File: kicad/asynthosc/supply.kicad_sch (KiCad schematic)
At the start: 37 parts, among them J1 USB_B_Micro, J2 Conn_02x05_Odd_Even, U1 LM1117S-3.3, U11 LM1117S-5.0, U12 Si1869DH, U7 USBLC6-2SC6, U9 LMR62421XMF

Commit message: wip
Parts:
- removed C46: 10u, symbol Device:C
- added C46: 10u, Capacitor_SMD:CP_Elec_4x5.4, symbol Device:C_Polarized
- F1: footprint (none) -> Resistor_SMD:R_0805_2012Metric
- FB1: footprint (none) -> Inductor_SMD:L_0402_1005Metric
- TH1: footprint (none) -> Resistor_THT:R_Axial_DIN0204_L3.6mm_D1.6mm_P7.62mm_Horizontal
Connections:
- net GND: now also C46.2
- net USB_VBUS: now also C46.1
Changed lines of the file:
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@@
 	)
 	(symbol
+		(lib_id "Device:C_Polarized")
+		(at 41.91 180.34 0)
+		(unit 1)
+		(exclude_from_sim no)
+		(in_bom yes)
+		(on_board yes)
+		(dnp no)
+		(fields_autoplaced yes)
+		(property "Reference" "C46"
+			(at 45.72 178.1809 0)
+			(effects
+				(font
+					(size 1.27 1.27)
+				)
+				(justify left)
+			)
+		)
+		(property "Value" "10u"
+			(at 45.72 180.7209 0)
+			(effects
+				(font
+					(size 1.27 1.27)
+				)
+				(justify left)
+			)
+		)
+		(property "Footprint" "Capacitor_SMD:CP_Elec_4x5.4"
+			(at 42.8752 184.15 0)
+			(effects
+				(font
+					(size 1.27 1.27)
+				)
+				(hide yes)
+			)
+		)
+		(property "Datasheet" "~"
+			(at 41.91 180.34 0)
+			(effects
+				(font
+					(size 1.27 1.27)
+				)
+				(hide yes)
+			)
+		)
+		(property "Description" "Polarized capacitor"
+			(at 41.91 180.34 0)
+			(effects
+				(font
+					(size 1.27 1.27)
+				)
+				(hide yes)
+			)
+		)
+		(pin "1"
+		)
+		(pin "2"
+		)
+		(instances
+			(project "asynthosc"
+				(path "/d73e377a-a016-415f-8824-91cc6e4907b9/22ca5166-338c-4a24-8f8a-545e4a0286bf"
+					(reference "C46")
+					(unit 1)
+				)
+			)
+		)
+	)
+	(symbol
 		(lib_id "Device:C")
 		(at 91.44 213.36 0)
@@
 	)
 	(symbol
-		(lib_id "Device:C")
-		(at 41.91 180.34 0)
-		(unit 1)
-		(exclude_from_sim yes)
-		(in_bom yes)
-		(on_board yes)
-		(dnp no)
-		(property "Reference" "C46"
-			(at 34.036 178.816 0)
-			(effects
-				(font
-					(size 1.27 1.27)
-				)
-				(justify left)
-			)
-		)
-		(property "Value" "10u"
-			(at 34.036 181.356 0)
-			(effects
-				(font
-					(size 1.27 1.27)
-				)
-				(justify left)
-			)
-		)
-		(property "Footprint" ""
-			(at 42.8752 184.15 0)
-			(effects
-				(font
-					(size 1.27 1.27)
-				)
-				(hide yes)
-			)
-		)
-		(property "Datasheet" "~"
-			(at 41.91 180.34 0)
-			(effects
-				(font
-					(size 1.27 1.27)
-				)
-				(hide yes)
-			)
-		)
-		(property "Description" "Unpolarized capacitor"
-			(at 41.91 180.34 0)
-			(effects
-				(font
-					(size 1.27 1.27)
-				)
-				(hide yes)
-			)
-		)
-		(pin "2"
-		)
-		(pin "1"
-		)
-		(instances
-			(project "asynthosc"
-				(path "/d73e377a-a016-415f-8824-91cc6e4907b9/22ca5166-338c-4a24-8f8a-545e4a0286bf"
-					(reference "C46")
-					(unit 1)
-				)
-			)
-		)
-	)
-	(symbol
 		(lib_id "Diode:ESD9B5.0ST5G")
 		(at 67.31 57.15 90)
@@
 			)
 		)
-		(property "Footprint" ""
+		(property "Footprint" "Resistor_SMD:R_0805_2012Metric"
 			(at 134.62 44.958 90)
 			(effects
@@
 			)
 		)
-		(property "Footprint" ""
+		(property "Footprint" "Resistor_THT:R_Axial_DIN0204_L3.6mm_D1.6mm_P7.62mm_Horizontal"
 			(at 143.51 43.18 0)
 			(effects
@@
 			)
 		)
-		(property "Footprint" ""
+		(property "Footprint" "Inductor_SMD:L_0402_1005Metric"
 			(at 165.1 44.958 90)
 			(effects

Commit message: sch: change stm32 for smaller one, create smaller jumper footprint
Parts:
- C1, C14, C2, C3, C4, C47, C48, C52, C53, TH1: RefNum (none) -> _generic_
- D1, D3: Manufacturer (none) -> OnSemi
- D17, D18, D7: Manufacturer (none) -> Vishay; RefNum (none) -> SS24
- D2: Manufacturer (none) -> Guangdong
- F1: RefNum ASMD0805-125 -> (none)
- FB1: Manufacturer (none) -> Murata; RefNum (none) -> BLM15PX330SN1D
- J1: Manufacturer (none) -> ShouHan; RefNum (none) -> MicroXNJ
- JP11, JP9: footprint Jumper:SolderJumper-2_P1.3mm_Open_Pad1.0x1.5mm -> Resistor_SMD:R_0402_1005Metric
- L1: Manufacturer (none) -> Xiangru
- U1: Manufacturer (none) -> TI; RefNum (none) -> LM1117S-3.3
- U11: Manufacturer (none) -> Diodes Inc; RefNum (none) -> ZLDO1117
- U12: RefNum (none) -> Si1869DH
- U7: Manufacturer (none) -> ST; RefNum (none) -> USBLC6-2SC6
- U9: Manufacturer (none) -> TI; RefNum (none) -> LMR62421XMF

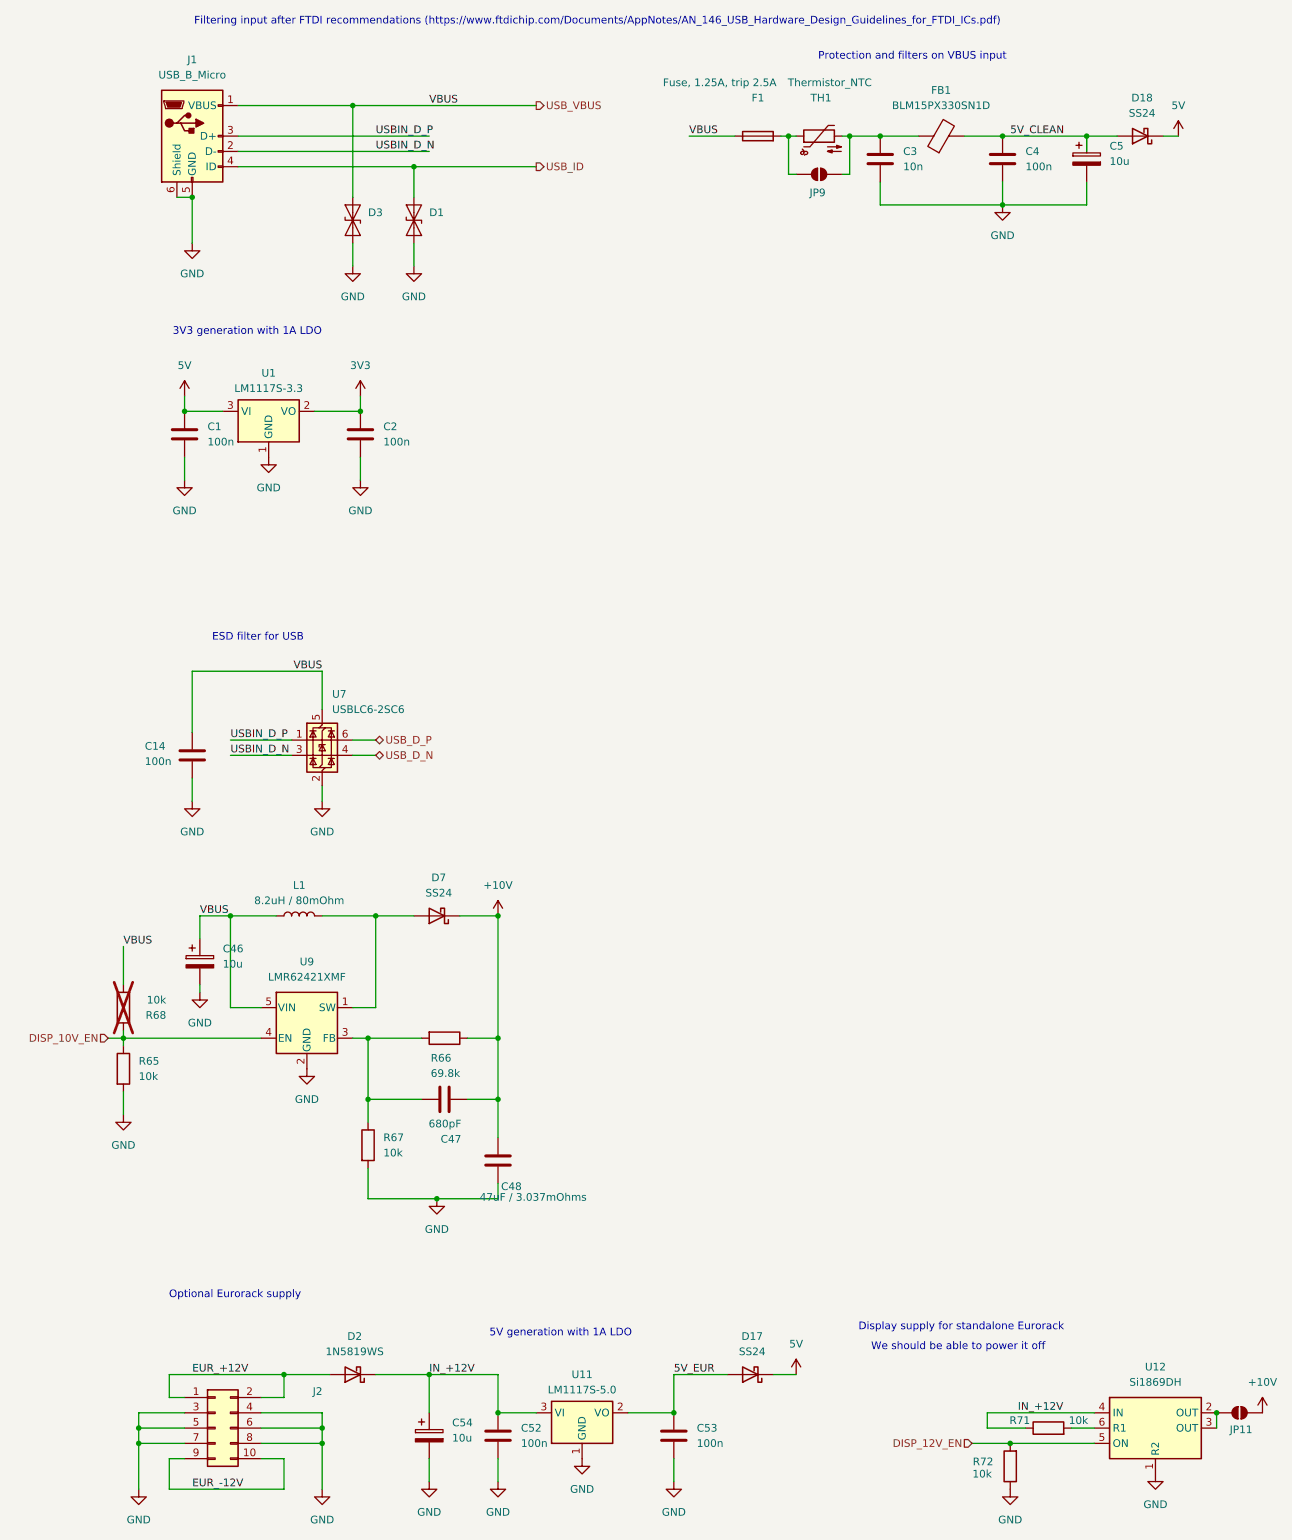
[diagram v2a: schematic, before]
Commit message: bom: update bom for lcsc
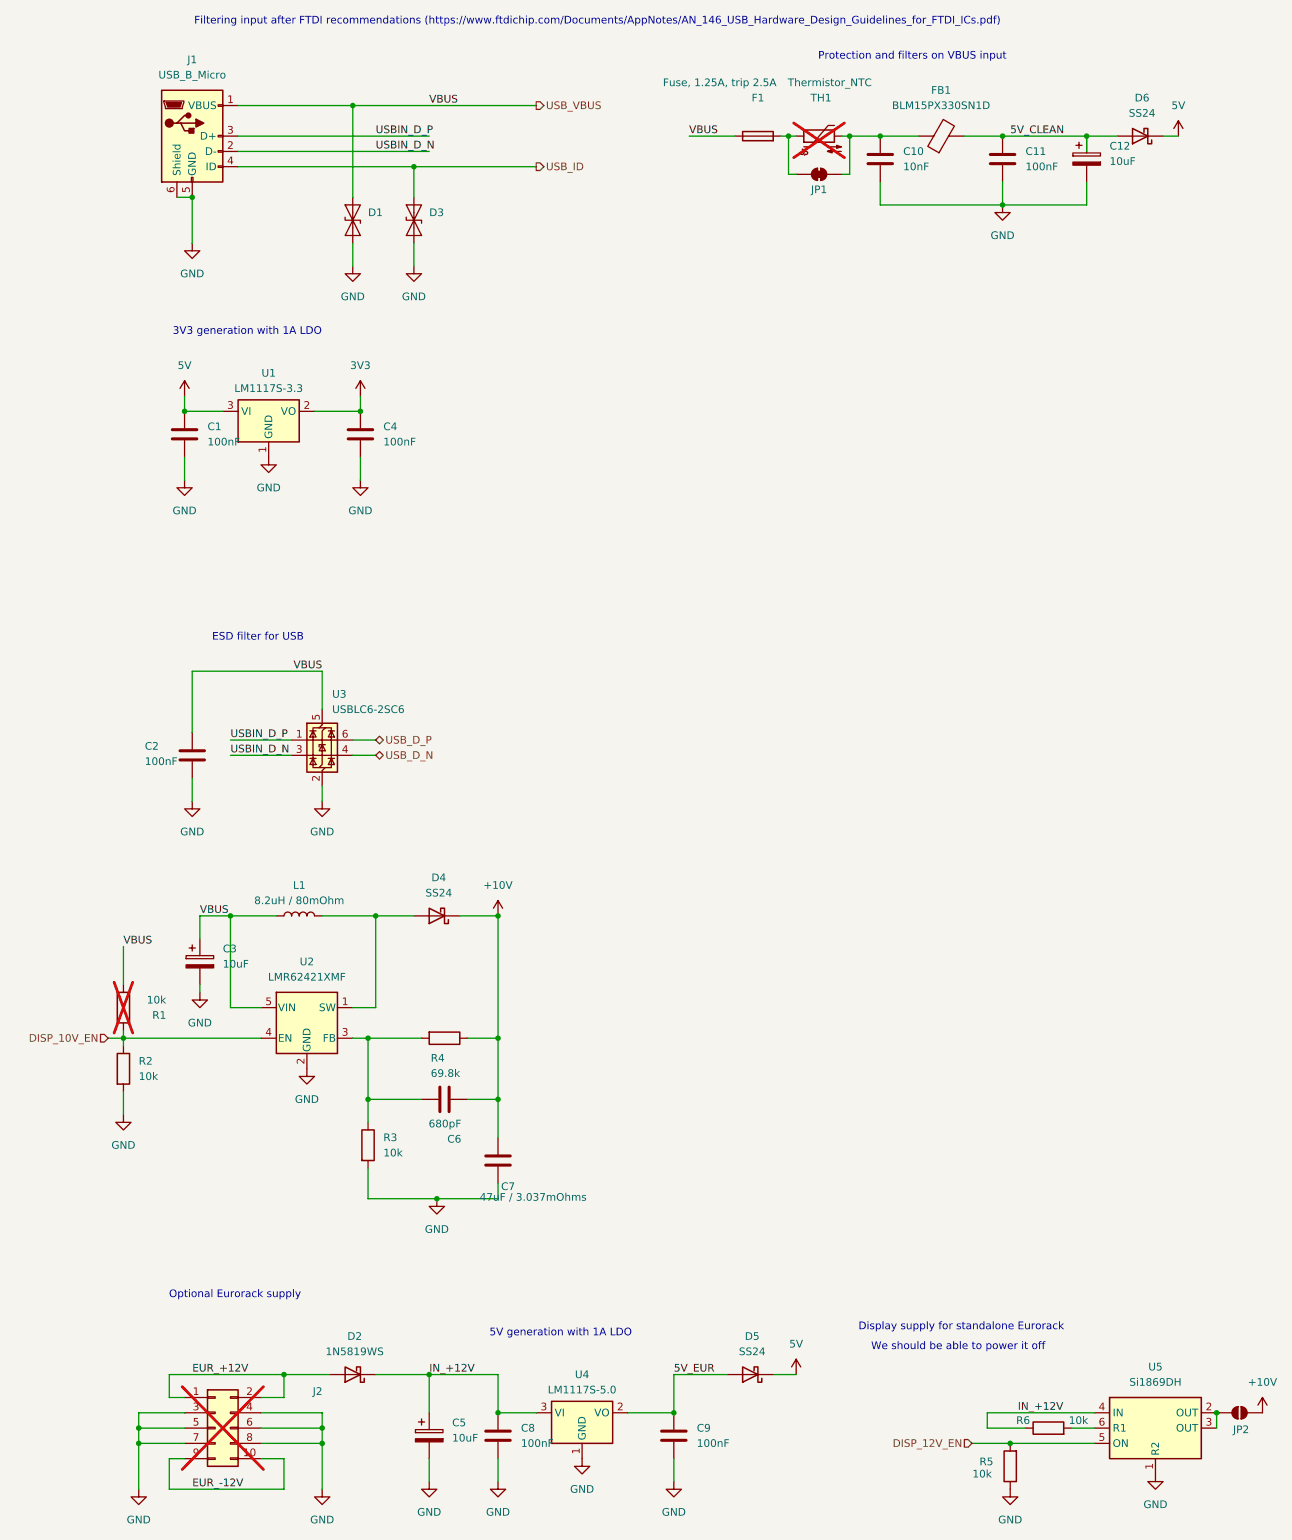
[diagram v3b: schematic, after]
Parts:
- removed JP9: SolderJumper_2_Open, Resistor_SMD:R_0402_1005Metric, symbol Jumper:SolderJumper_2_Open
- added JP1: SolderJumper_2_Bridged, symbol Jumper:SolderJumper_2_Bridged
- C1: value 100n -> 100nF
- C10: renamed from C3; value 10n -> 10nF
- C11: renamed from C4; value 100n -> 100nF
- C12: renamed from C5; value 10u -> 10uF; Manufacturer (none) -> Roqang; RefNum (none) -> RVT1V100M0405
- C2: renamed from C14; value 100n -> 100nF
- C3: renamed from C46; value 10u -> 10uF; Manufacturer (none) -> Roqang; RefNum (none) -> RVT1V100M0405
- C4: renamed from C2; value 100n -> 100nF
- C5: renamed from C54; value 10u -> 10uF; Manufacturer (none) -> Roqang; RefNum (none) -> RVT1V100M0405
- C8: renamed from C52; value 100n -> 100nF
- C9: renamed from C53; value 100n -> 100nF
- D1: renamed from D3; RefNum (none) -> ESD9B5.0ST5G
- D2: RefNum (none) -> 1N5819WS
- D3: renamed from D1; RefNum (none) -> ESD9B5.0ST5G
- D4: renamed from D7; Manufacturer Vishay -> Fosan
- D5: renamed from D17; Manufacturer Vishay -> Fosan
- D6: renamed from D18; Manufacturer Vishay -> Fosan
- F1: RefNum (none) -> _generic_
- J2: RefNum (none) -> _na_; now not fitted
- JP2: renamed from JP11; RefNum (none) -> _na_
- R1: renamed from R68; RefNum (none) -> _generic_
- R2: renamed from R65; RefNum (none) -> _generic_
- R3: renamed from R67; RefNum (none) -> _generic_
- R4: renamed from R66; RefNum (none) -> _generic_
- R5: renamed from R72; RefNum (none) -> _generic_
- R6: renamed from R71; RefNum (none) -> _generic_
- TH1: now not fitted
- U1: footprint Package_TO_SOT_SMD:TO-263-3_TabPin2 -> Package_TO_SOT_SMD:SOT-223; Manufacturer TI -> HTC Korea; RefNum LM1117S-3.3 -> LM1117S-3.3
- U3: renamed from U7; Manufacturer ST -> STMicroelectronics
- U4: renamed from U11; footprint Package_TO_SOT_SMD:TO-263-3_TabPin2 -> Package_TO_SOT_SMD:SOT-223; Manufacturer Diodes Inc -> HTC Korea; RefNum ZLDO1117 -> LM1117S-5.0
- renumbered C47 to C6, C48 to C7, U9 to U2, U12 to U5
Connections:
- net at C10.1, FB1.1, TH1.2: now also JP1.2 (B)
- net at F1.2, TH1.1: now also JP1.1 (A)

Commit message: pcb: placing
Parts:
- added H1, H2, H3: MountingHole_Pad, MountingHole:MountingHole_2.2mm_M2_Pad, symbol Mechanical:MountingHole_Pad
- added TP19, TP2, TP20, TP21, TP22, TP23, TP3, TP4: TestPoint, TestPoint:TestPoint_Pad_D1.0mm, symbol Connector:TestPoint
- C8, C9: footprint Capacitor_SMD:C_0402_1005Metric -> Capacitor_SMD:C_0805_2012Metric
- JP1: footprint (none) -> asynthosc:SolderJumper_0402_1005Metric_Bridged
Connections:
- net +10V: now also TP3.1
- net 5V: now also TP2.1
- net 5V_EUR: now also TP4.1
- net GND: now also H1.1, H2.1, H3.1, TP19.1, TP20.1, TP21.1, TP22.1, TP23.1
